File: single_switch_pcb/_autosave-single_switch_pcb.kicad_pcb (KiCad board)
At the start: 2 copper layers, 6 parts, among them J1 Conn_01x01_Female, J2 Conn_01x01_Female, J3 Conn_01x01_Female, J4 Conn_01x01_Female, U1 switchsocket

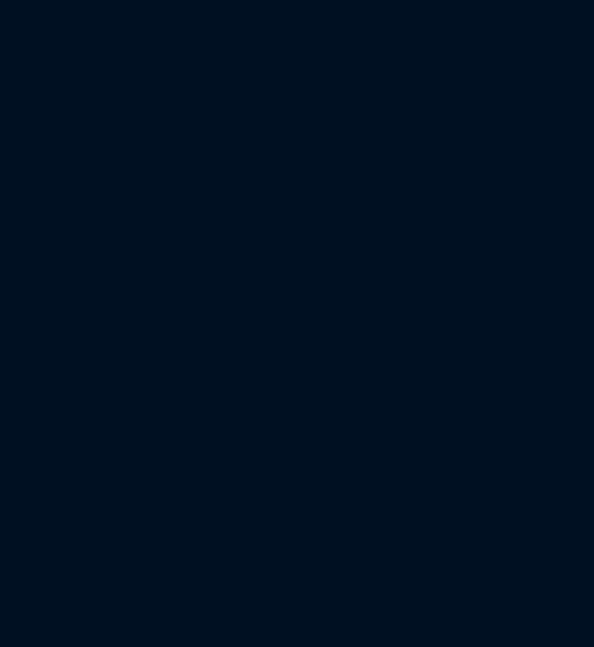
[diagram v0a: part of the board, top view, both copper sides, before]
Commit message: added 5 pin switch mechanical drawing. make pcb support 5 pins
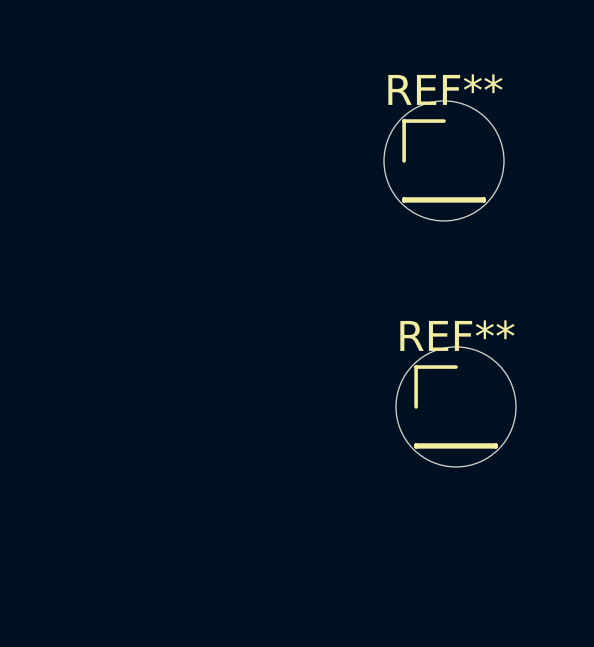
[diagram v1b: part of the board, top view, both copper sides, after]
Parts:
- added REF**: PinHeader_1x01_P2.54mm_Vertical, Connector_PinHeader_2.54mm:PinHeader_1x01_P2.54mm_Vertical, F.Cu at (192.7, 92.6)
- added REF**: PinHeader_1x01_P2.54mm_Vertical, Connector_PinHeader_2.54mm:PinHeader_1x01_P2.54mm_Vertical, F.Cu at (192.3, 84.4)
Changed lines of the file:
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@@
     (tracks 19)
     (zones 0)
-    (modules 6)
+    (modules 8)
     (nets 4)
   )
@@
     (mod_text_size 1 1)
     (mod_text_width 0.15)
-    (pad_size 1.524 1.524)
-    (pad_drill 0.762)
+    (pad_size 4 4)
+    (pad_drill 4)
     (pad_to_mask_clearance 0)
     (aux_axis_origin 0 0)
@@
     (add_net "Net-(J1-Pad1)")
   )
+  (module Connector_PinHeader_2.54mm:PinHeader_1x01_P2.54mm_Vertical (layer F.Cu)
+    (at 192.7 92.6)
+    (descr "Through hole straight pin header, 1x01, 2.54mm pitch, single row")
+    (tags "Through hole pin header THT 1x01 2.54mm single row")
+    (fp_text reference REF** (at 0 -2.33) (layer F.SilkS)
+      (effects (font (size 1 1) (thickness 0.15)))
+    )
+    (fp_text value PinHeader_1x01_P2.54mm_Vertical (at 0 2.33) (layer F.Fab)
+      (effects (font (size 1 1) (thickness 0.15)))
+    )
+    (fp_line (start -0.635 -1.27) (end 1.27 -1.27) (layer F.Fab) (width 0.1))
+    (fp_line (start 1.27 -1.27) (end 1.27 1.27) (layer F.Fab) (width 0.1))
+    (fp_line (start 1.27 1.27) (end -1.27 1.27) (layer F.Fab) (width 0.1))
+    (fp_line (start -1.27 1.27) (end -1.27 -0.635) (layer F.Fab) (width 0.1))
+    (fp_line (start -1.27 -0.635) (end -0.635 -1.27) (layer F.Fab) (width 0.1))
+    (fp_line (start -1.33 1.33) (end 1.33 1.33) (layer F.SilkS) (width 0.12))
+    (fp_line (start -1.33 1.27) (end -1.33 1.33) (layer F.SilkS) (width 0.12))
+    (fp_line (start 1.33 1.27) (end 1.33 1.33) (layer F.SilkS) (width 0.12))
+    (fp_line (start -1.33 1.27) (end 1.33 1.27) (layer F.SilkS) (width 0.12))
+    (fp_line (start -1.33 0) (end -1.33 -1.33) (layer F.SilkS) (width 0.12))
+    (fp_line (start -1.33 -1.33) (end 0 -1.33) (layer F.SilkS) (width 0.12))
+    (fp_line (start -1.8 -1.8) (end -1.8 1.8) (layer F.CrtYd) (width 0.05))
+    (fp_line (start -1.8 1.8) (end 1.8 1.8) (layer F.CrtYd) (width 0.05))
+    (fp_line (start 1.8 1.8) (end 1.8 -1.8) (layer F.CrtYd) (width 0.05))
+    (fp_line (start 1.8 -1.8) (end -1.8 -1.8) (layer F.CrtYd) (width 0.05))
+    (fp_text user %R (at 0 0 90) (layer F.Fab)
+      (effects (font (size 1 1) (thickness 0.15)))
+    )
+    (pad "" np_thru_hole circle (at 0 0) (size 4 4) (drill 4) (layers *.Cu *.Mask))
+    (model ${KISYS3DMOD}/Connector_PinHeader_2.54mm.3dshapes/PinHeader_1x01_P2.54mm_Vertical.wrl
+      (at (xyz 0 0 0))
+      (scale (xyz 1 1 1))
+      (rotate (xyz 0 0 0))
+    )
+  )
+  (module Connector_PinHeader_2.54mm:PinHeader_1x01_P2.54mm_Vertical (layer F.Cu)
+    (at 192.3 84.4)
+    (descr "Through hole straight pin header, 1x01, 2.54mm pitch, single row")
+    (tags "Through hole pin header THT 1x01 2.54mm single row")
+    (fp_text reference REF** (at 0 -2.33) (layer F.SilkS)
+      (effects (font (size 1 1) (thickness 0.15)))
+    )
+    (fp_text value PinHeader_1x01_P2.54mm_Vertical (at 0 2.33) (layer F.Fab)
+      (effects (font (size 1 1) (thickness 0.15)))
+    )
+    (fp_text user %R (at 0 0 90) (layer F.Fab)
+      (effects (font (size 1 1) (thickness 0.15)))
+    )
+    (fp_line (start -0.635 -1.27) (end 1.27 -1.27) (layer F.Fab) (width 0.1))
+    (fp_line (start 1.27 -1.27) (end 1.27 1.27) (layer F.Fab) (width 0.1))
+    (fp_line (start 1.27 1.27) (end -1.27 1.27) (layer F.Fab) (width 0.1))
+    (fp_line (start -1.27 1.27) (end -1.27 -0.635) (layer F.Fab) (width 0.1))
+    (fp_line (start -1.27 -0.635) (end -0.635 -1.27) (layer F.Fab) (width 0.1))
+    (fp_line (start -1.33 1.33) (end 1.33 1.33) (layer F.SilkS) (width 0.12))
+    (fp_line (start -1.33 1.27) (end -1.33 1.33) (layer F.SilkS) (width 0.12))
+    (fp_line (start 1.33 1.27) (end 1.33 1.33) (layer F.SilkS) (width 0.12))
+    (fp_line (start -1.33 1.27) (end 1.33 1.27) (layer F.SilkS) (width 0.12))
+    (fp_line (start -1.33 0) (end -1.33 -1.33) (layer F.SilkS) (width 0.12))
+    (fp_line (start -1.33 -1.33) (end 0 -1.33) (layer F.SilkS) (width 0.12))
+    (fp_line (start -1.8 -1.8) (end -1.8 1.8) (layer F.CrtYd) (width 0.05))
+    (fp_line (start -1.8 1.8) (end 1.8 1.8) (layer F.CrtYd) (width 0.05))
+    (fp_line (start 1.8 1.8) (end 1.8 -1.8) (layer F.CrtYd) (width 0.05))
+    (fp_line (start 1.8 -1.8) (end -1.8 -1.8) (layer F.CrtYd) (width 0.05))
+    (pad "" np_thru_hole circle (at 0 0) (size 4 4) (drill 4) (layers *.Cu *.Mask))
+    (model ${KISYS3DMOD}/Connector_PinHeader_2.54mm.3dshapes/PinHeader_1x01_P2.54mm_Vertical.wrl
+      (at (xyz 0 0 0))
+      (scale (xyz 1 1 1))
+      (rotate (xyz 0 0 0))
+    )
+  )
   (module "hotswapsocket:hotswap socket" (layer F.Cu)
